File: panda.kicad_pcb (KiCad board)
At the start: 4 copper layers, 100 x 130 mm, 266 parts, among them J1 Conn_01x02, J10 Conn_01x02, J11 4-Pin Load Cell, J12 5-Pin Load Cell, J13 Conn_02x01, J14 Conn_01x02, J15 Conn_01x02, J16 Conn_01x02, J17 Conn_01x02, J18 Conn_01x02, J19 Conn_01x02, J2 Conn_02x01, J20 395934308, J3 Conn_02x01, J4 USB_C_Receptacle_USB2.0_16P, J5 Conn_01x02, J6 Conn_01x02, J7 Conn_01x02, J8 Conn_01x02, J9 Conn_01x02, K1 G5Q-1A DC24, K2 G5Q-1 DC24, K3 G5Q-1 DC24, Q1 BSS138, Q10 BSS138, Q11 BSS138, Q2 BSS138, Q3 DMP6023LE-13, Q4 BSS138, Q5 BSS138, Q6 BSS138, Q7 BSS138, Q8 BSS138, Q9 BSS138, SW1 USAKRO UK-B0227-G4.3-B-250, SW2 USAKRO UK-B0227-G4.3-B-250, U1 LM3880-1AA, U10 ADS112C04, U11 ADS112C04, U12 INA187A1, U13 ADS112C04, U2 LMR33630BDDA, U3 TPS78533QKVURQ1, U4 TLC555xPS, U5 TPS78450QDBVRQ1, U6 LM66200DRLR, U7 ESP32-S3-WROOM-1U, U8 ADS112C04, U9 ADS112C04

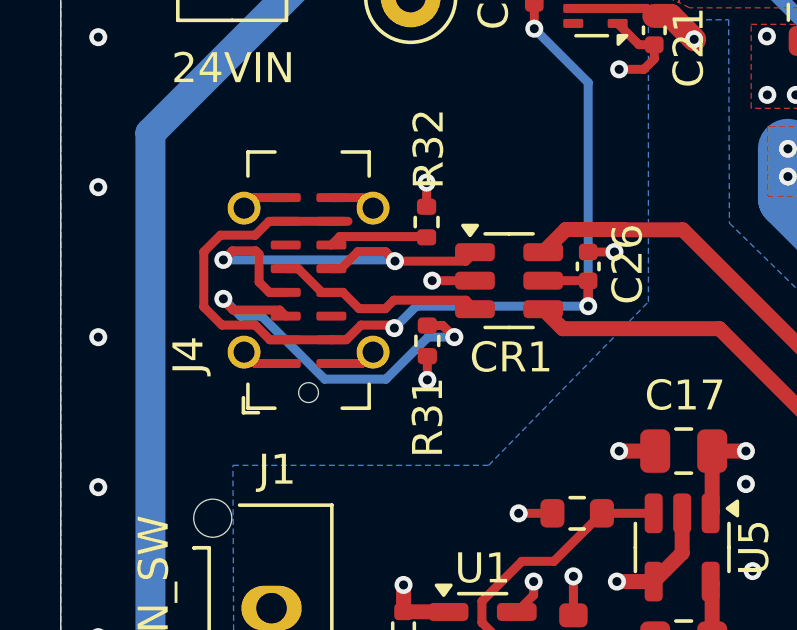
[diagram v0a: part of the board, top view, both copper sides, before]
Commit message: fix usb data traces on pcb
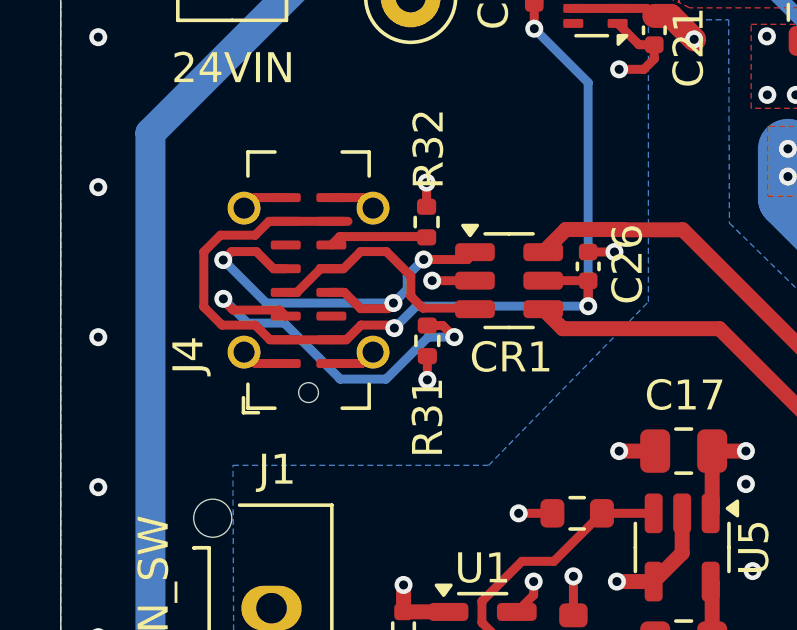
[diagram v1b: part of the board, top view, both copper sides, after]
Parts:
- R75: value 25m 1W -> 10m 1W
- U12: value INA187A1 -> INA187A2
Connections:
- CR1 pad 1: /ESP32 Breakout/D+ -> /ESP32 Breakout/D-
- CR1 pad 3: /ESP32 Breakout/D- -> /ESP32 Breakout/D+
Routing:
- net /ESP32 Breakout/D-: track 7.10 -> 15.2 mm, vias 0 -> 3
- net /ESP32 Breakout/D+: track 14.3 -> 8.06 mm, vias 2 -> 0

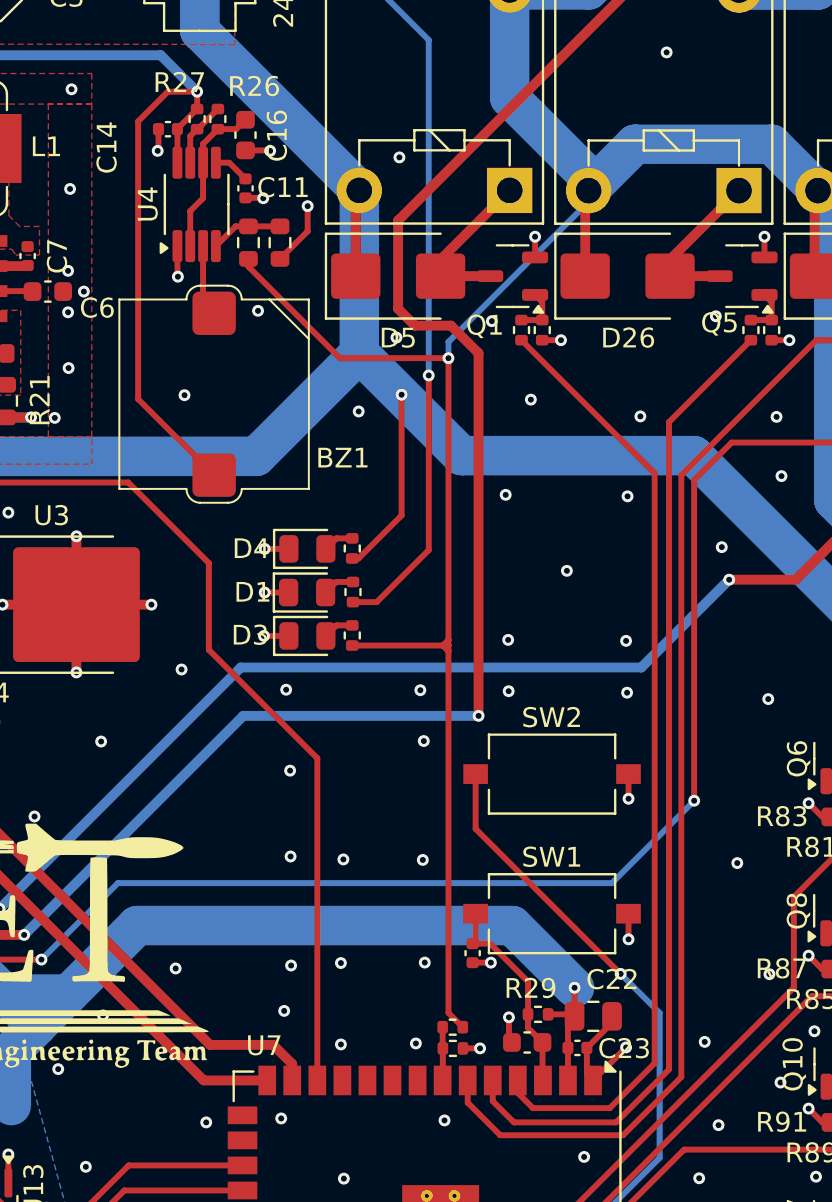
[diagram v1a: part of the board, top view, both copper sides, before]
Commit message: add nmos to buzzer to keep off when 24vSAFE off
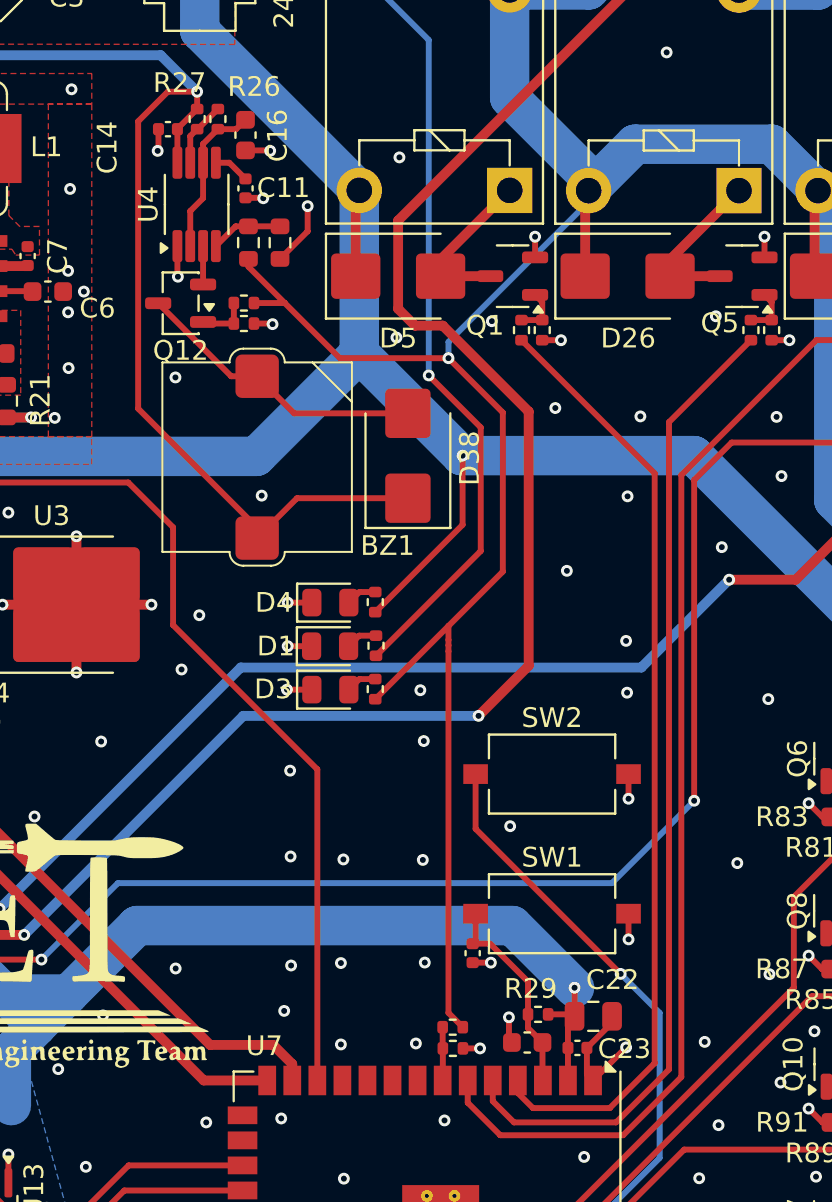
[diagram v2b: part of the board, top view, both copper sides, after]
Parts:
- added D38: SK44BL, Diode_SMD:D_SMB, F.Cu at (159.3, 63.6)
- added Q12: BSS138, Package_TO_SOT_SMD:SOT-23-3, F.Cu at (147.8, 55.8)
- added R98: 10k, Resistor_SMD:R_0402_1005Metric, F.Cu at (151.0, 55.8)
- added R99: 2.2k, Resistor_SMD:R_0402_1005Metric, F.Cu at (151.0, 56.9)
- moved BZ1 3.86 mm to (156.4, 68.4)
- moved R11 2.96 mm to (157.6, 75.4)
- moved R13 2.96 mm to (157.6, 71.0)
- moved D1 2.96 mm to (155.3, 73.2)
- moved D3 2.96 mm to (155.3, 75.4)
- moved D4 2.96 mm to (155.3, 71.0)
- moved R9 2.96 mm to (157.7, 73.2)
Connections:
- U4 pad 3: Net-(BZ1--) -> Net-(Q12-S)
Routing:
- net /Power Regulation/+5.3V: track 79.5 -> 91.1 mm
- net Net-(BZ1--): track 3.64 -> 15.0 mm
- net /Power Regulation/+24V_POST_LCKT: track 62.3 -> 66.0 mm
- net +24V_SAFE: track 170.6 -> 174.0 mm
- net Net-(Q12-G): track 0.00 -> 2.63 mm
- net Net-(Q12-S): track 0.00 -> 1.94 mm
- net IGN_RESIST_READ: track 109.2 -> 111.1 mm
- net GND: track 207.8 -> 208.7 mm, vias 368 -> 366

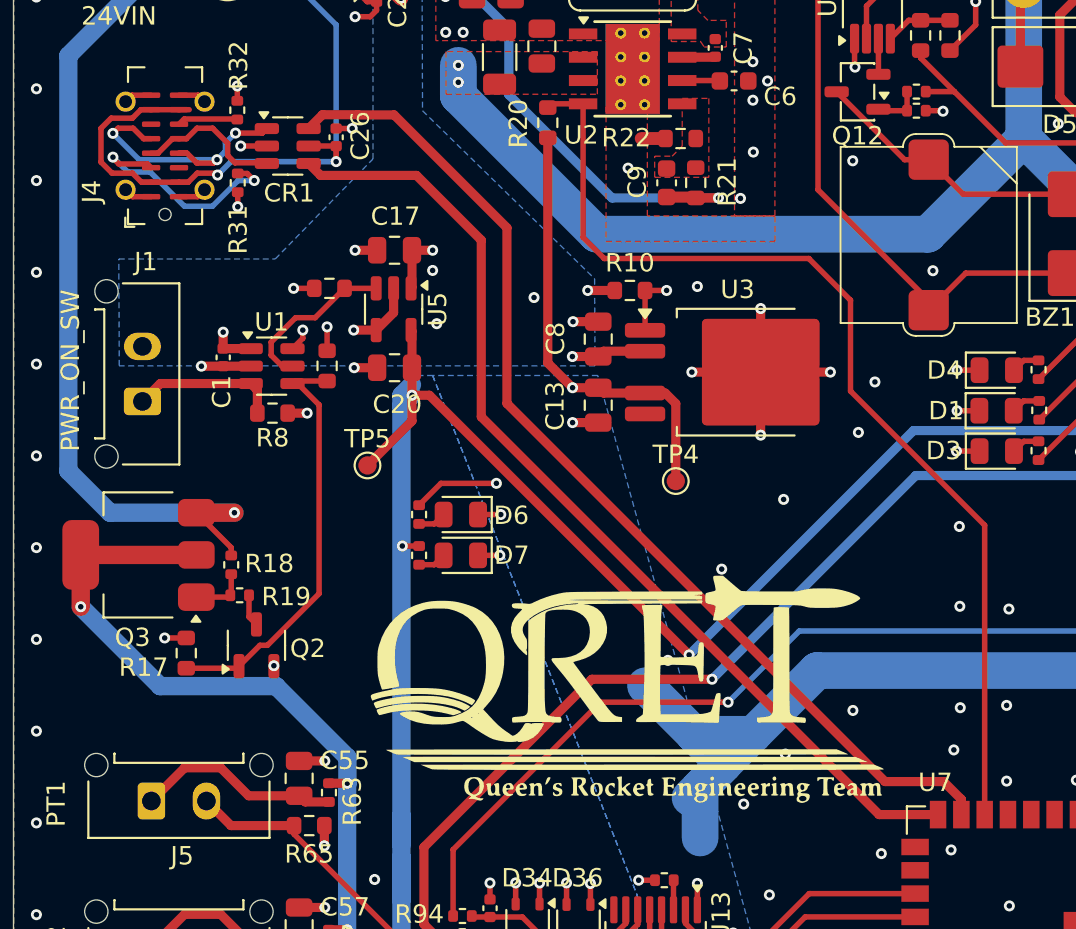
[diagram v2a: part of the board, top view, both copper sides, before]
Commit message: fix usb traces to be 90 ohms impedance
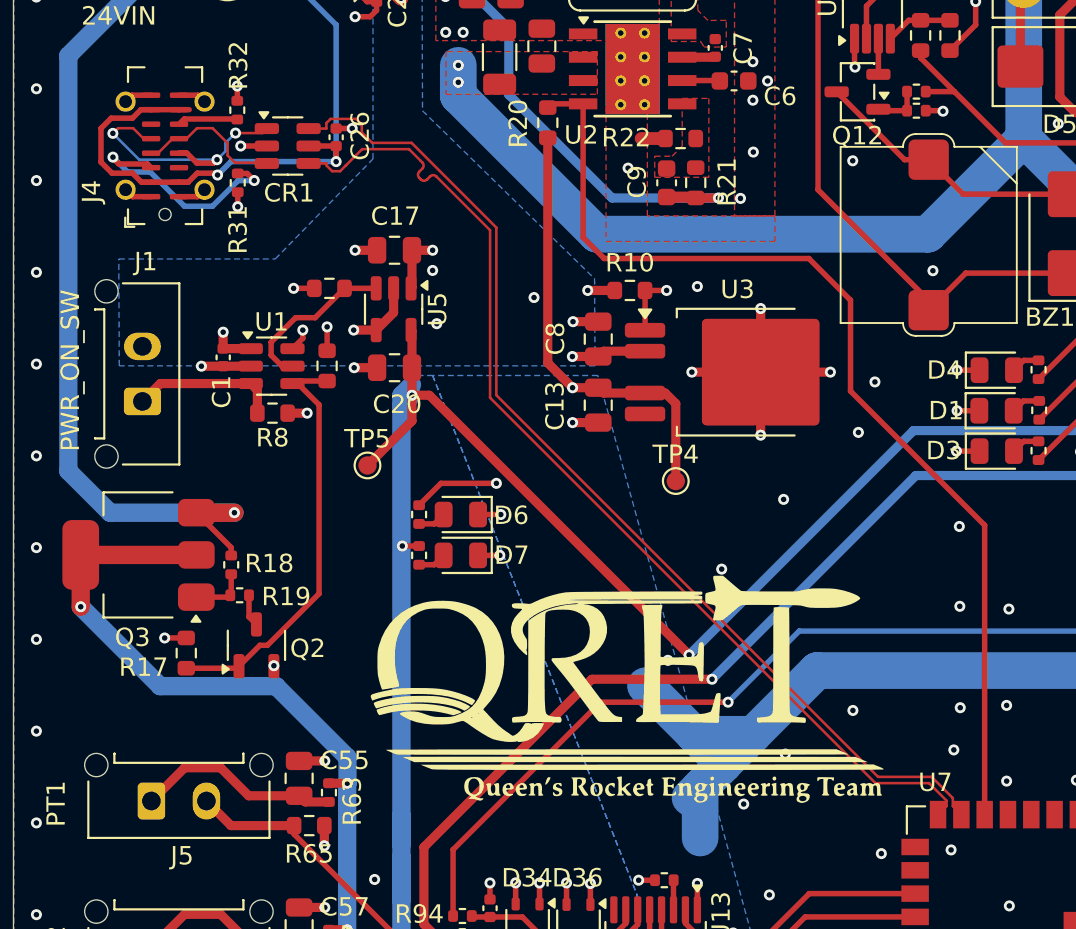
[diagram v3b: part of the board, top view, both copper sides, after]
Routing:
- net /ESP32 Breakout/USB_P: track 54.6 -> 57.5 mm
